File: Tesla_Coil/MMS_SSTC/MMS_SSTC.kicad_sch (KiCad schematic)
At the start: 26 parts, among them J2 Screw_Terminal_01x02, Q1 FQA8N100C, U1 NE555P, U2 UCC37322P, U3 CD74HC14E

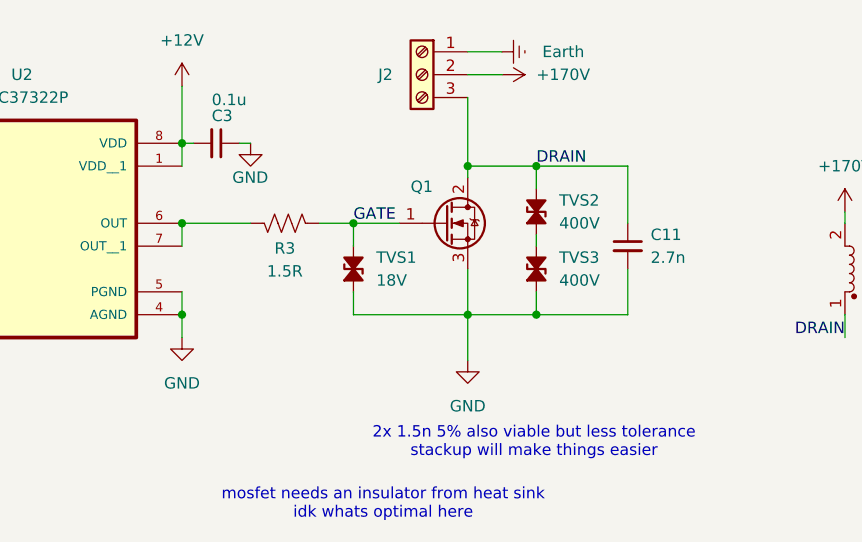
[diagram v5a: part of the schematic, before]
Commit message: finish acrylic case minus final tolerances
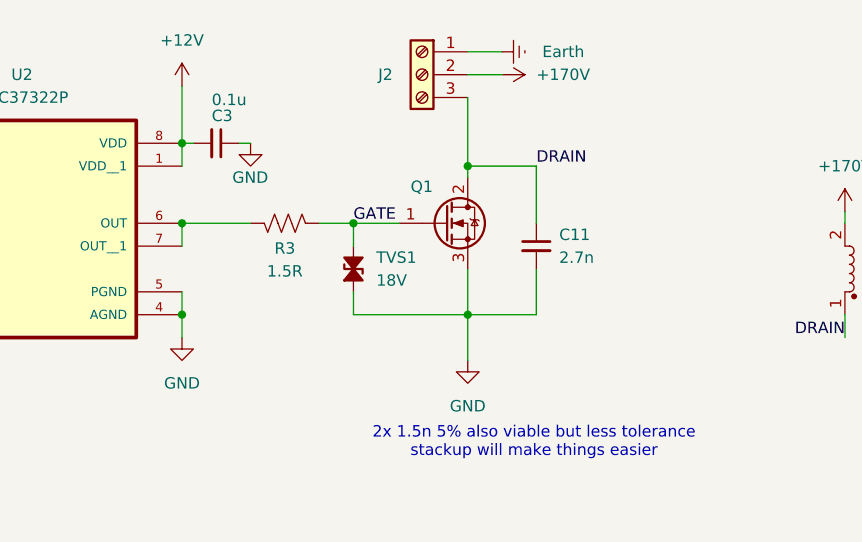
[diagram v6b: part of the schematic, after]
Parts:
- removed TVS2, TVS3: 400V, Diode_THT:D_DO-27_P12.70mm_Horizontal, symbol Device:D_TVS_Small_Filled
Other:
- note removed: "mosfet needs an insulator from heat sink idk whats optimal here"
- moved on the sheet: C11
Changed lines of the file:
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@@
 		(comment 2 "Designed by William Layne")
 	)
-	(text "mosfet needs an insulator from heat sink\nidk whats optimal here"
-		(exclude_from_sim no)
-		(at 155.702 162.052 0)
-		(effects
-			(font
-				(size 1.27 1.27)
-			)
-		)
-	)
 	(text "2x 1.5n 5% also viable but less tolerance \nstackup will make things easier"
 		(exclude_from_sim no)
@@
 	)
 	(junction
-		(at 172.72 124.46)
-		(diameter 0)
-		(color 0 0 0 0)
-	)
-	(junction
 		(at 58.42 52.07)
 		(diameter 0)
@@
 	)
 	(junction
-		(at 172.72 140.97)
-		(diameter 0)
-		(color 0 0 0 0)
-	)
-	(junction
 		(at 133.35 130.81)
 		(diameter 0)
@@
 	(wire
 		(pts
-			(xy 182.88 124.46) (xy 182.88 130.81)
+			(xy 172.72 124.46) (xy 172.72 130.81)
 		)
 		(stroke
@@
 	(wire
 		(pts
-			(xy 182.88 135.89) (xy 182.88 140.97)
+			(xy 172.72 135.89) (xy 172.72 140.97)
 		)
 		(stroke
@@
 	(wire
 		(pts
-			(xy 172.72 140.97) (xy 182.88 140.97)
-		)
-		(stroke
-			(width 0)
-			(type default)
-		)
-	)
-	(wire
-		(pts
 			(xy 86.36 68.58) (xy 86.36 69.85)
 		)
@@
 	(wire
 		(pts
-			(xy 172.72 124.46) (xy 182.88 124.46)
-		)
-		(stroke
-			(width 0)
-			(type default)
-		)
-	)
-	(wire
-		(pts
 			(xy 133.35 140.97) (xy 133.35 143.51)
 		)
@@
 	(wire
 		(pts
-			(xy 172.72 138.43) (xy 172.72 140.97)
-		)
-		(stroke
-			(width 0)
-			(type default)
-		)
-	)
-	(wire
-		(pts
 			(xy 39.37 74.93) (xy 39.37 68.58)
 		)
@@
 	(wire
 		(pts
-			(xy 172.72 124.46) (xy 172.72 127)
-		)
-		(stroke
-			(width 0)
-			(type default)
-		)
-	)
-	(wire
-		(pts
-			(xy 172.72 133.35) (xy 172.72 132.08)
-		)
-		(stroke
-			(width 0)
-			(type default)
-		)
-	)
-	(wire
-		(pts
 			(xy 86.36 48.26) (xy 86.36 58.42)
 		)
@@
 	)
 	(symbol
-		(lib_id "Device:D_TVS_Small_Filled")
-		(at 172.72 129.54 90)
-		(unit 1)
-		(exclude_from_sim no)
-		(in_bom yes)
-		(on_board yes)
-		(dnp no)
-		(property "Reference" "TVS2"
-			(at 175.26 128.2699 90)
-			(effects
-				(font
-					(size 1.27 1.27)
-				)
-				(justify right)
-			)
-		)
-		(property "Value" "400V"
-			(at 175.26 130.8099 90)
-			(effects
-				(font
-					(size 1.27 1.27)
-				)
-				(justify right)
-			)
-		)
-		(property "Footprint" "Diode_THT:D_DO-27_P12.70mm_Horizontal"
-			(at 172.72 129.54 0)
-			(effects
-				(font
-					(size 1.27 1.27)
-				)
-				(hide yes)
-			)
-		)
-		(property "Datasheet" "~"
-			(at 172.72 129.54 0)
-			(effects
-				(font
-					(size 1.27 1.27)
-				)
-				(hide yes)
-			)
-		)
-		(property "Description" "Bidirectional transient-voltage-suppression diode, small symbol, filled shape"
-			(at 172.72 129.54 0)
-			(effects
-				(font
-					(size 1.27 1.27)
-				)
-				(hide yes)
-			)
-		)
-		(property "DKPN" "1.5KE400CALFCT-ND"
-			(at 172.72 129.54 90)
-			(effects
-				(font
-					(size 1.27 1.27)
-				)
-				(hide yes)
-			)
-		)
-		(pin "1"
-		)
-		(pin "2"
-		)
-		(instances
-			(project "MMS_SSTC"
-				(path "/b29a3901-c128-4c19-b69f-61de71283b43"
-					(reference "TVS2")
-					(unit 1)
-				)
-			)
-		)
-	)
-	(symbol
 		(lib_id "power:+5V")
 		(at 207.01 129.54 0)
@@
 	)
 	(symbol
-		(lib_id "Device:D_TVS_Small_Filled")
-		(at 172.72 135.89 90)
-		(unit 1)
-		(exclude_from_sim no)
-		(in_bom yes)
-		(on_board yes)
-		(dnp no)
-		(property "Reference" "TVS3"
-			(at 175.26 134.6199 90)
-			(effects
-				(font
-					(size 1.27 1.27)
-				)
-				(justify right)
-			)
-		)
-		(property "Value" "400V"
-			(at 175.26 137.1599 90)
-			(effects
-				(font
-					(size 1.27 1.27)
-				)
-				(justify right)
-			)
-		)
-		(property "Footprint" "Diode_THT:D_DO-27_P12.70mm_Horizontal"
-			(at 172.72 135.89 0)
-			(effects
-				(font
-					(size 1.27 1.27)
-				)
-				(hide yes)
-			)
-		)
-		(property "Datasheet" "~"
-			(at 172.72 135.89 0)
-			(effects
-				(font
-					(size 1.27 1.27)
-				)
-				(hide yes)
-			)
-		)
-		(property "Description" "Bidirectional transient-voltage-suppression diode, small symbol, filled shape"
-			(at 172.72 135.89 0)
-			(effects
-				(font
-					(size 1.27 1.27)
-				)
-				(hide yes)
-			)
-		)
-		(property "DKPN" "1.5KE400CALFCT-ND"
-			(at 172.72 135.89 90)
-			(effects
-				(font
-					(size 1.27 1.27)
-				)
-				(hide yes)
-			)
-		)
-		(pin "1"
-		)
-		(pin "2"
-		)
-		(instances
-			(project ""
-				(path "/b29a3901-c128-4c19-b69f-61de71283b43"
-					(reference "TVS3")
-					(unit 1)
-				)
-			)
-		)
-	)
-	(symbol
 		(lib_id "Device:L_Coupled")
 		(at 209.55 135.89 90)
@@
 	(symbol
 		(lib_id "Device:C_Small")
-		(at 182.88 133.35 0)
+		(at 172.72 133.35 0)
 		(unit 1)
 		(exclude_from_sim no)
@@
 		(fields_autoplaced yes)
 		(property "Reference" "C11"
-			(at 185.42 132.0862 0)
+			(at 175.26 132.0862 0)
 			(effects
 				(font
@@
 		)
 		(property "Value" "2.7n"
-			(at 185.42 134.6262 0)
+			(at 175.26 134.6262 0)
 			(effects
 				(font
@@
 		)
 		(property "Footprint" "Capacitor_THT:C_Rect_L13.0mm_W4.0mm_P10.00mm_FKS3_FKP3_MKS4"
-			(at 182.88 133.35 0)
+			(at 172.72 133.35 0)
 			(effects
 				(font
@@
 		)
 		(property "Datasheet" "~"
-			(at 182.88 133.35 0)
+			(at 172.72 133.35 0)
 			(effects
 				(font
@@
 		)
 		(property "Description" "Unpolarized capacitor, small symbol"
-			(at 182.88 133.35 0)
+			(at 172.72 133.35 0)
 			(effects
 				(font
@@
 		)
 		(property "DKPN" "495-3207-ND"
-			(at 182.88 133.35 0)
+			(at 172.72 133.35 0)
 			(effects
 				(font

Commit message: make it use a vishay trimpot fuck you bourns
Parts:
- RV1: DKPN 3296X-502LF-ND -> T93XA-5.0K-ND
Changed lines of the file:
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@@
 			)
 		)
-		(property "DKPN" "3296X-502LF-ND"
+		(property "DKPN" "T93XA-5.0K-ND"
 			(at 149.86 64.77 0)
 			(effects
